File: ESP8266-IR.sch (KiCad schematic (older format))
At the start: 7 parts

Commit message: Initial commit.
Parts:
- added C4: 10uF, Capacitors_ThroughHole:C_Disc_D7.5_P5, symbol C
- added D1, D2, D3, D4: LED, LEDs:LED-5MM, symbol LED
- added IC1: ATTINY85-P, Housings_DIP:DIP-8_W7.62mm_LongPads, symbol ATTINY85-P
- added JP1, JP2: Jumper_NO_Small, Pin_Headers:Pin_Header_Straight_1x02, symbol Jumper_NO_Small
- added P1: CONN_01X06, Pin_Headers:Pin_Header_Straight_1x06, symbol CONN_01X06
- added Q1, Q2: 2N2222A, TO_SOT_Packages_THT:TO-18_3Pin, symbol Q_NPN_EBC
- added R1, R4: 10k, Resistors_ThroughHole:Resistor_Horizontal_RM10mm, symbol R
- added SW1, SW2, SW3: SW_PUSH, Custom:PushbuttonSquare2pin, symbol SW_PUSH
- C1, C2: renamed from C?; footprint (none) -> Capacitors_ThroughHole:C_Disc_D7.5_P5
- CON1: renamed from CON?; footprint (none) -> Connect:BARREL_JACK
- R2, R3: renamed from R?; footprint (none) -> Resistors_ThroughHole:Resistor_Horizontal_RM10mm
- U1: renamed from U?; footprint SOT-223 -> TO_SOT_Packages_THT:TO-220_Neutral123_Horizontal_LargePads
- U2: renamed from U?; footprint (none) -> adafruit:ESP-12
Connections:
- net +3V3: now also C4.2, D1.2 (A), D2.2 (A), D3.2 (A), D4.2 (A), JP1.1, JP2.1, P1.4 (P4), R1.1; no longer U2.8 (VCC)
- net ESP_RST: now also R1.2, SW3.2
- net ESP_RXD: now also P1.3 (P3)
- net ESP_TXD: now also P1.2 (P2)
- net GND: now also C4.1, IC1.4 (GND), P1.6 (P6), Q1.1 (E), Q2.1 (E), R4.2, SW1.1, SW2.1, SW3.1
- net GPIO0: now also SW2.2
- net VIN: now reaches C1.1, CON1.1, U1.3 (VI)
- net GPIO12: no longer names the net of U2.6 (GPIO12)
- net GPIO13: no longer names the net of U2.7 (GPIO13)
- net GPIO15: no longer names the net of U2.10 (GPIO15)
- net GPIO15: now also R4.1
- new net: JP2.2, U2.8 (VCC)
- new net: IC1.8 (VCC), JP1.2
- new net: D1.1 (K), D2.1 (K), Q1.3 (C)
- new net: D3.1 (K), D4.1 (K), Q2.3 (C)
- new net ATT_RST: IC1.1 (PB5(~RESET~/dW/ADC0/PCINT5)), SW1.2
- new net IR_OUT: IC1.6 (PB1(MISO/DO/AIN1/OC0B/OC1A/PCINT1)), Q1.2 (B), Q2.2 (B)
- no-connect marks 0 -> 1
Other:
- moved on the sheet: R2, R3, U2

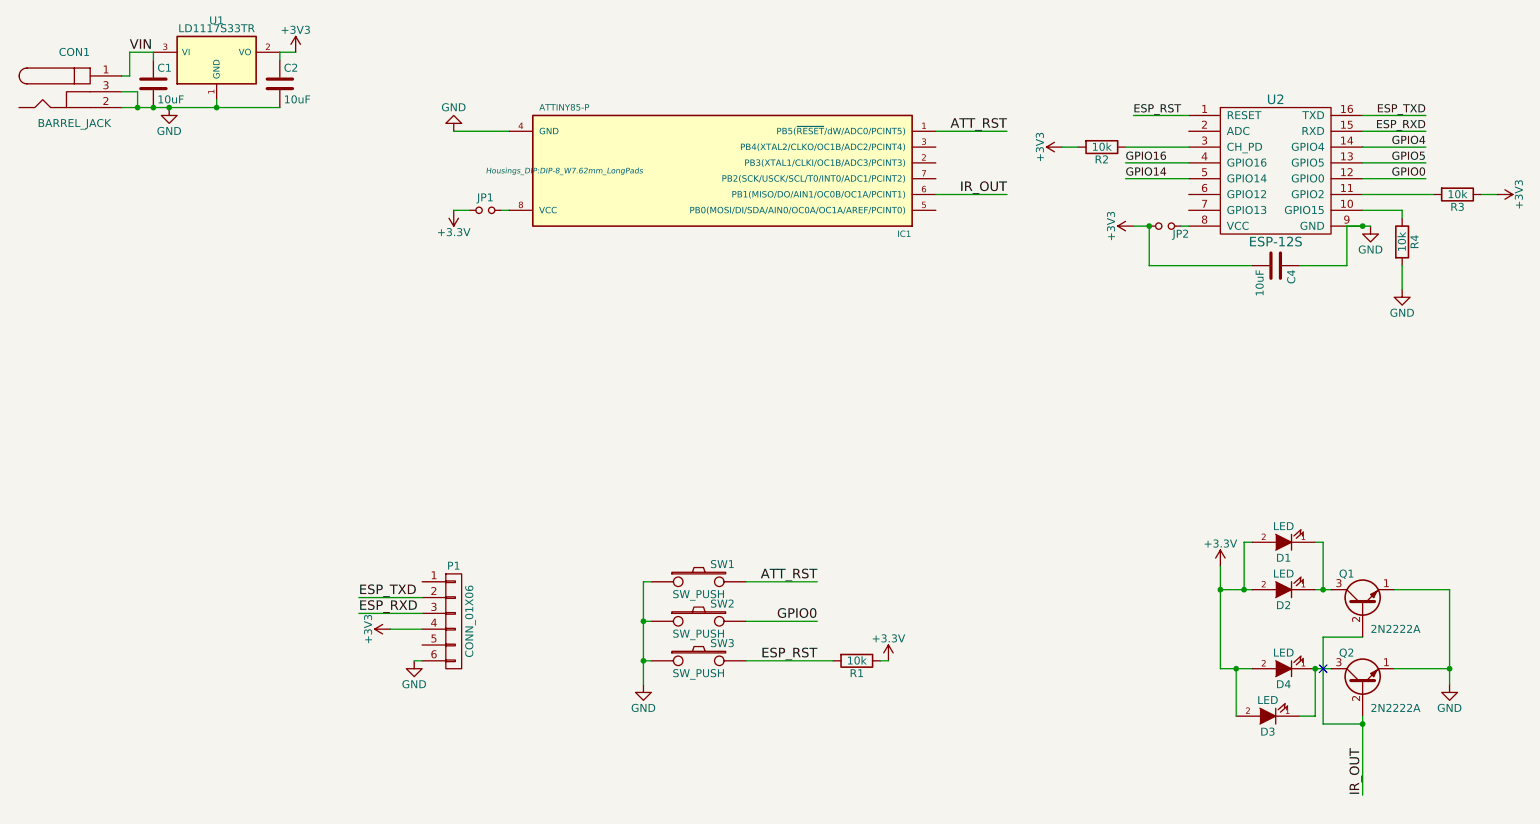
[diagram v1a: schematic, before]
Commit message: Removed ATTINY coprocessor.
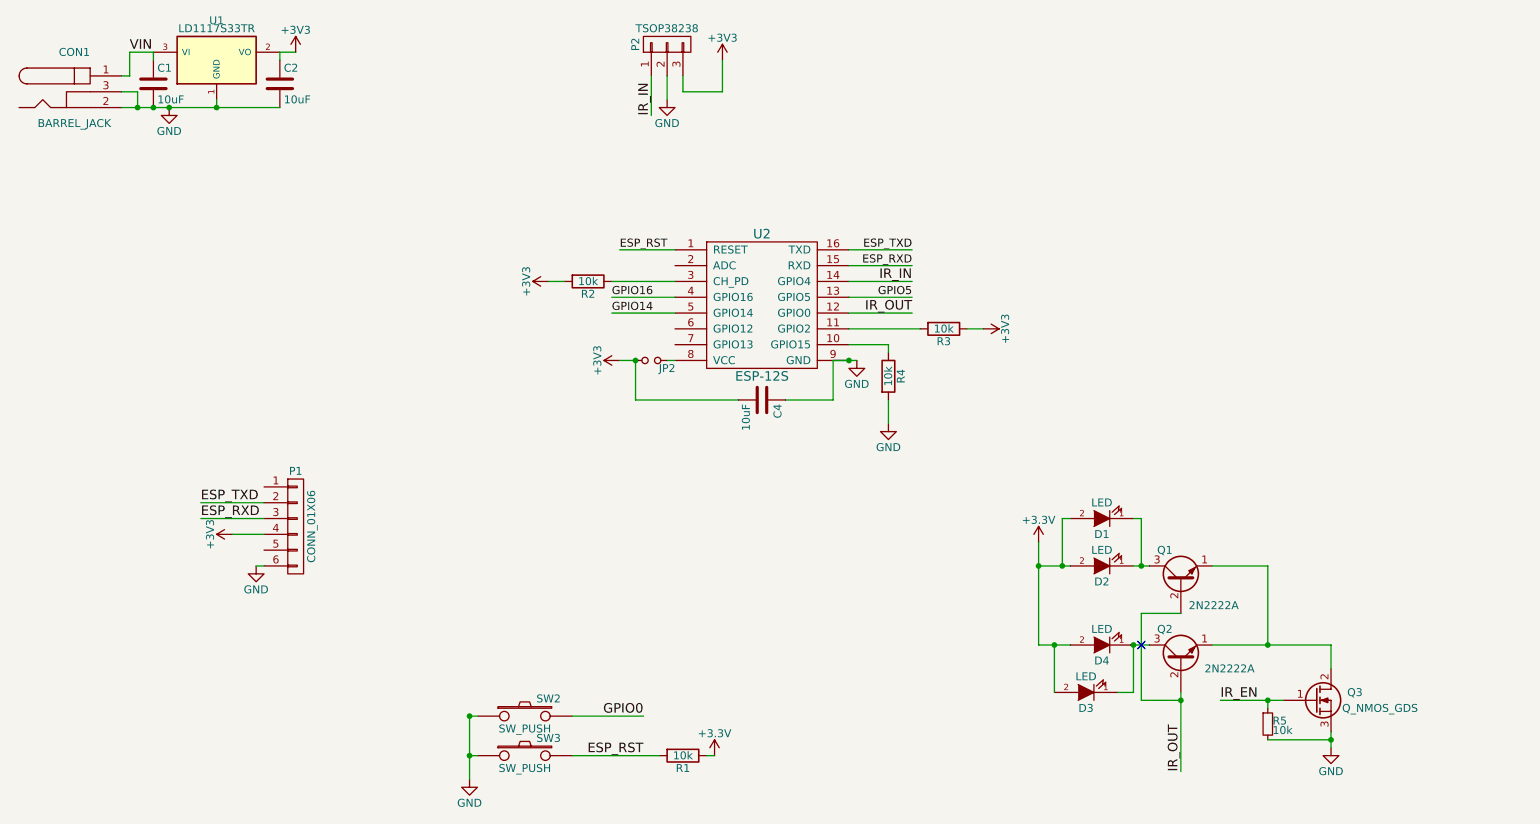
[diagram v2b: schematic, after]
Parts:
- removed IC1: ATTINY85-P, Housings_DIP:DIP-8_W7.62mm_LongPads, symbol ATTINY85-P
- removed JP1: Jumper_NO_Small, Pin_Headers:Pin_Header_Straight_1x02, symbol Jumper_NO_Small
- removed SW1: SW_PUSH, Custom:PushbuttonSquare2pin, symbol SW_PUSH
- added P2: TSOP38238, symbol CONN_01X03
- added Q3: Q_NMOS_GDS, symbol Q_NMOS_GDS
- added R5: 10k, symbol R_Small
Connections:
- net +3V3: now also P2.3 (P3)
- net GND: now also P2.2 (P2), Q3.3 (S), R5.2; no longer Q1.1 (E), Q2.1 (E)
- net GPIO0: no longer U2.12 (GPIO0)
- net IR_OUT: now also U2.12 (GPIO0)
- net GPIO4 renamed IR_IN
- net IR_IN: now also P2.1 (P1)
- new net: Q1.1 (E), Q2.1 (E), Q3.2 (D)
- new net IR_EN: Q3.1 (G), R5.1
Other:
- moved on the sheet: C4, D1, D2, D3, D4, JP2, P1, Q1, Q2, R1, R2, R3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

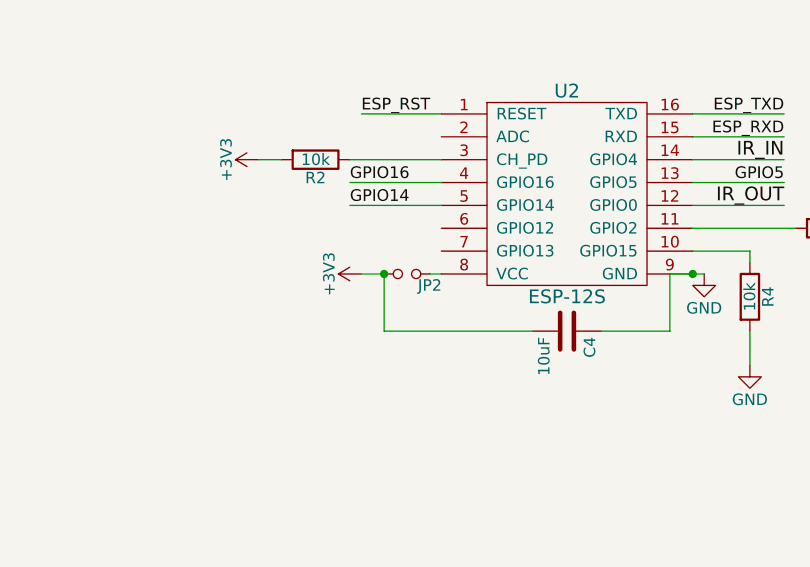
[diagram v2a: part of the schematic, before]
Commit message: Changed footpints.
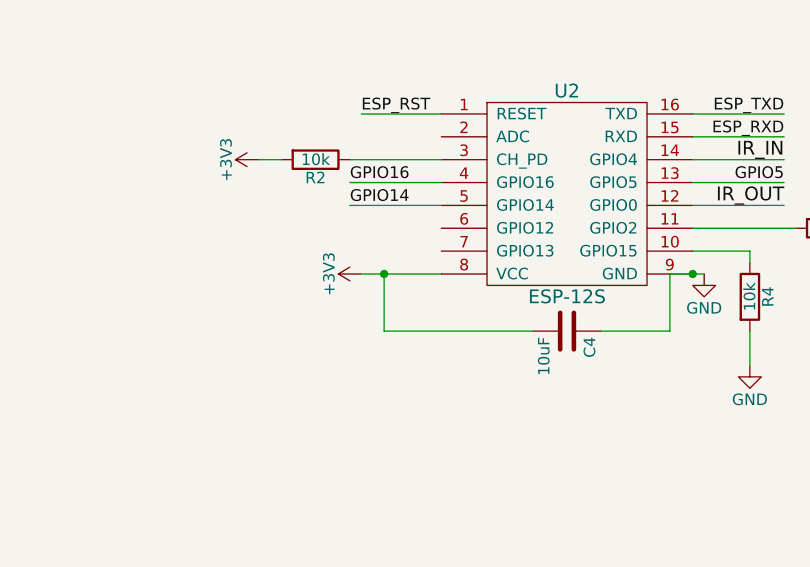
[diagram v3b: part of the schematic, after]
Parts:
- removed JP2: Jumper_NO_Small, Pin_Headers:Pin_Header_Straight_1x02, symbol Jumper_NO_Small
- C1, C2, C4: footprint Capacitors_ThroughHole:C_Disc_D7.5_P5 -> Capacitors_SMD:C_1206
- P2: footprint (none) -> Pin_Headers:Pin_Header_Straight_1x03
- Q3: footprint (none) -> Custom:SOT-223
- R1, R2, R3, R4: footprint Resistors_ThroughHole:Resistor_Horizontal_RM10mm -> Resistors_SMD:R_1206
- R5: footprint (none) -> Resistors_SMD:R_1206
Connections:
- net +3V3: now also U2.8 (VCC)
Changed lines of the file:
@@
 $EndComp
 $Comp
-L GND #PWR8
+L GND #PWR01
 U 1 1 584AEB9D
 P 6150 2950
-F 0 "#PWR8" H 6150 2700 50  0001 C CNN
+F 0 "#PWR01" H 6150 2700 50  0001 C CNN
 F 1 "GND" H 6150 2800 50  0000 C CNN
 F 2 "" H 6150 2950 50  0000 C CNN
@@
 $EndComp
 $Comp
-L +3V3 #PWR7
+L +3V3 #PWR02
 U 1 1 584AEBB3
 P 4650 2950
-F 0 "#PWR7" H 4650 2800 50  0001 C CNN
+F 0 "#PWR02" H 4650 2800 50  0001 C CNN
 F 1 "+3V3" H 4650 3090 50  0000 C CNN
 F 2 "" H 4650 2950 50  0000 C CNN
@@
 F 0 "R2" V 4530 2450 50  0000 C CNN
 F 1 "10k" V 4450 2450 50  0000 C CNN
-F 2 "Resistors_ThroughHole:Resistor_Horizontal_RM10mm" V 4380 2450 50  0001 C CNN
+F 2 "Resistors_SMD:R_1206" V 4380 2450 50  0001 C CNN
 F 3 "" H 4450 2450 50  0000 C CNN
 	1    4450 2450
@@
 $EndComp
 $Comp
-L +3V3 #PWR5
+L +3V3 #PWR03
 U 1 1 584AEC43
 P 4200 2450
-F 0 "#PWR5" H 4200 2300 50  0001 C CNN
+F 0 "#PWR03" H 4200 2300 50  0001 C CNN
 F 1 "+3V3" H 4200 2590 50  0000 C CNN
 F 2 "" H 4200 2450 50  0000 C CNN
@@
 F 0 "R3" V 6780 2750 50  0000 C CNN
 F 1 "10k" V 6700 2750 50  0000 C CNN
-F 2 "Resistors_ThroughHole:Resistor_Horizontal_RM10mm" V 6630 2750 50  0001 C CNN
+F 2 "Resistors_SMD:R_1206" V 6630 2750 50  0001 C CNN
 F 3 "" H 6700 2750 50  0000 C CNN
 	1    6700 2750
@@
 $EndComp
 $Comp
-L +3V3 #PWR6
+L +3V3 #PWR04
 U 1 1 584AECDE
 P 6950 2750
-F 0 "#PWR6" H 6950 2600 50  0001 C CNN
+F 0 "#PWR04" H 6950 2600 50  0001 C CNN
 F 1 "+3V3" H 6950 2890 50  0000 C CNN
 F 2 "" H 6950 2750 50  0000 C CNN
@@
 $EndComp
 $Comp
-L +3V3 #PWR1
+L +3V3 #PWR05
 U 1 1 584B2A57
 P 2600 1000
-F 0 "#PWR1" H 2600 850 50  0001 C CNN
+F 0 "#PWR05" H 2600 850 50  0001 C CNN
 F 1 "+3V3" H 2600 1140 50  0000 C CNN
 F 2 "" H 2600 1000 50  0000 C CNN
@@
 $EndComp
 $Comp
-L GND #PWR4
+L GND #PWR06
 U 1 1 584B2A8E
 P 1800 1350
-F 0 "#PWR4" H 1800 1100 50  0001 C CNN
+F 0 "#PWR06" H 1800 1100 50  0001 C CNN
 F 1 "GND" H 1800 1200 50  0000 C CNN
 F 2 "" H 1800 1350 50  0000 C CNN
@@
 F 0 "C1" H 1725 1300 50  0000 L CNN
 F 1 "10uF" H 1725 1100 50  0000 L CNN
-F 2 "Capacitors_ThroughHole:C_Disc_D7.5_P5" H 1738 1050 50  0001 C CNN
+F 2 "Capacitors_SMD:C_1206" H 1738 1050 50  0001 C CNN
 F 3 "" H 1700 1200 50  0000 C CNN
 	1    1700 1200
@@
 F 0 "C2" H 2525 1300 50  0000 L CNN
 F 1 "10uF" H 2525 1100 50  0000 L CNN
-F 2 "Capacitors_ThroughHole:C_Disc_D7.5_P5" H 2538 1050 50  0001 C CNN
+F 2 "Capacitors_SMD:C_1206" H 2538 1050 50  0001 C CNN
 F 3 "" H 2500 1200 50  0000 C CNN
 	1    2500 1200
@@
 $EndComp
 $Comp
-L GND #PWR15
+L GND #PWR07
 U 1 1 584B6DE3
 P 3700 5600
-F 0 "#PWR15" H 3700 5350 50  0001 C CNN
+F 0 "#PWR07" H 3700 5350 50  0001 C CNN
 F 1 "GND" H 3700 5450 50  0000 C CNN
 F 2 "" H 3700 5600 60  0000 C CNN
@@
 F 0 "R1" V 5130 5450 50  0000 C CNN
 F 1 "10k" V 5050 5450 50  0000 C CNN
-F 2 "Resistors_ThroughHole:Resistor_Horizontal_RM10mm" V 4980 5450 30  0001 C CNN
+F 2 "Resistors_SMD:R_1206" V 4980 5450 30  0001 C CNN
 F 3 "" H 5050 5450 30  0000 C CNN
 	1    5050 5450
@@
 $EndComp
 $Comp
-L +3.3V #PWR14
+L +3.3V #PWR08
 U 1 1 584B735B
 P 5250 5450
-F 0 "#PWR14" H 5250 5300 50  0001 C CNN
+F 0 "#PWR08" H 5250 5300 50  0001 C CNN
 F 1 "+3.3V" H 5250 5590 50  0000 C CNN
 F 2 "" H 5250 5450 60  0000 C CNN
@@
 F 0 "C4" H 5575 3300 50  0000 L CNN
 F 1 "10uF" H 5575 3100 50  0000 L CNN
-F 2 "Capacitors_ThroughHole:C_Disc_D7.5_P5" H 5588 3050 30  0001 C CNN
+F 2 "Capacitors_SMD:C_1206" H 5588 3050 30  0001 C CNN
 F 3 "" H 5550 3200 60  0000 C CNN
 	1    5550 3200
@@
 Connection ~ 4750 2950
 $Comp
-L GND #PWR9
+L GND #PWR09
 U 1 1 584BB1BB
 P 6350 3350
-F 0 "#PWR9" H 6350 3100 50  0001 C CNN
+F 0 "#PWR09" H 6350 3100 50  0001 C CNN
 F 1 "GND" H 6350 3200 50  0000 C CNN
 F 2 "" H 6350 3350 60  0000 C CNN
@@
 F 0 "R4" V 6430 3050 50  0000 C CNN
 F 1 "10k" V 6350 3050 50  0000 C CNN
-F 2 "Resistors_ThroughHole:Resistor_Horizontal_RM10mm" V 6280 3050 30  0001 C CNN
+F 2 "Resistors_SMD:R_1206" V 6280 3050 30  0001 C CNN
 F 3 "" H 6350 3050 30  0000 C CNN
 	1    6350 3050
@@
 $EndComp
 $Comp
-L GND #PWR12
+L GND #PWR010
 U 1 1 584BD657
 P 2350 4250
-F 0 "#PWR12" H 2350 4000 50  0001 C CNN
+F 0 "#PWR010" H 2350 4000 50  0001 C CNN
 F 1 "GND" H 2350 4100 50  0000 C CNN
 F 2 "" H 2350 4250 60  0000 C CNN
@@
 $EndComp
 $Comp
-L GND #PWR13
+L GND #PWR011
 U 1 1 584C0476
 P 9150 5400
-F 0 "#PWR13" H 9150 5150 50  0001 C CNN
+F 0 "#PWR011" H 9150 5150 50  0001 C CNN
 F 1 "GND" H 9150 5250 50  0000 C CNN
 F 2 "" H 9150 5400 60  0000 C CNN
@@
 Connection ~ 7300 4250
 $Comp
-L +3.3V #PWR11
+L +3.3V #PWR012
 U 1 1 584C07AE
 P 7300 4100
-F 0 "#PWR11" H 7300 3950 50  0001 C CNN
+F 0 "#PWR012" H 7300 3950 50  0001 C CNN
 F 1 "+3.3V" H 7300 4240 50  0000 C CNN
 F 2 "" H 7300 4100 60  0000 C CNN
@@
 Text Label 8200 5550 1    60   ~ 0
 IR_OUT
-$Comp
-L Jumper_NO_Small JP2
-U 1 1 584C62D5
-P 4850 2950
-F 0 "JP2" H 4950 2900 50  0000 C CNN
-F 1 "Jumper_NO_Small" H 4860 2890 50  0001 C CNN
-F 2 "Pin_Headers:Pin_Header_Straight_1x02" H 4850 2950 60  0001 C CNN
-F 3 "" H 4850 2950 60  0000 C CNN
-	1    4850 2950
-	1    0    0    -1
-$EndComp
-Wire Wire Line
-	4650 2950 4750 2950
+Wire Wire Line
+	4650 2950 5000 2950
 Wire Wire Line
 	4750 2950 4750 3200
-Wire Wire Line
-	4950 2950 5000 2950
 Wire Wire Line
 	7950 4250 7950 3950
@@
 $EndComp
 $Comp
-L +3V3 #PWR10
+L +3V3 #PWR013
 U 1 1 584E0D51
 P 2200 4050
-F 0 "#PWR10" H 2200 3900 50  0001 C CNN
+F 0 "#PWR013" H 2200 3900 50  0001 C CNN
 F 1 "+3V3" H 2200 4190 50  0000 C CNN
 F 2 "" H 2200 4050 60  0000 C CNN
@@
 F 0 "P2" H 4950 1150 50  0000 C CNN
 F 1 "TSOP38238" V 5050 950 50  0000 C CNN
-F 2 "" H 4950 950 60  0000 C CNN
+F 2 "Pin_Headers:Pin_Header_Straight_1x03" H 4950 950 60  0001 C CNN
 F 3 "" H 4950 950 60  0000 C CNN
 	1    4950 950
@@
 $EndComp
 $Comp
-L GND #PWR3
+L GND #PWR014
 U 1 1 5852B3AF
 P 4950 1300
-F 0 "#PWR3" H 4950 1050 50  0001 C CNN
+F 0 "#PWR014" H 4950 1050 50  0001 C CNN
 F 1 "GND" H 4950 1150 50  0000 C CNN
 F 2 "" H 4950 1300 60  0000 C CNN
@@
 $EndComp
 $Comp
-L +3V3 #PWR2
+L +3V3 #PWR015
 U 1 1 5852B5BB
 P 5300 1050
-F 0 "#PWR2" H 5300 900 50  0001 C CNN
+F 0 "#PWR015" H 5300 900 50  0001 C CNN
 F 1 "+3V3" H 5300 1190 50  0000 C CNN
 F 2 "" H 5300 1050 60  0000 C CNN
@@
 F 0 "Q3" H 9350 5150 50  0000 R CNN
 F 1 "Q_NMOS_GDS" H 9700 5050 50  0000 R CNN
-F 2 "" H 9250 5200 29  0000 C CNN
+F 2 "Custom:SOT-223" H 9250 5200 29  0001 C CNN
 F 3 "" H 9050 5100 60  0000 C CNN
 	1    9050 5100
@@
 F 0 "R5" H 8780 5270 50  0000 L CNN
 F 1 "10k" H 8780 5210 50  0000 L CNN
-F 2 "" H 8750 5250 60  0000 C CNN
+F 2 "Resistors_SMD:R_1206" H 8750 5250 60  0001 C CNN
 F 3 "" H 8750 5250 60  0000 C CNN
 	1    8750 5250

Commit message: Complete relayout, more smoothing, two layer design.
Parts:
- added C3, C5: C, Capacitors_SMD:C_1206, symbol C
- P1: value CONN_01X06 -> CONN_01X05; footprint Pin_Headers:Pin_Header_Straight_1x06 -> Pin_Headers:Pin_Header_Straight_1x05; symbol CONN_01X06 -> CONN_01X05
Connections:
- net GPIO14 is gone; now on net IR_EN: U2.5 (GPIO14)
- net GPIO16 is gone; now on net IR_IN: U2.4 (GPIO16)
- net IR_OUT is gone; now on net GPIO0: Q1.2 (B), Q2.2 (B), U2.12 (GPIO0)
- net +3V3: now also P1.3 (P3), C3.1, C5.1; no longer P1.4 (P4)
- net ESP_RXD: now also P1.2 (P2); no longer P1.3 (P3)
- net ESP_TXD: now also P1.1 (P1); no longer P1.2 (P2)
- net GND: now also P1.5 (P5), C3.2, C5.2; no longer P1.6 (P6)
- net IR_IN: no longer U2.14 (GPIO4)
- net GPIO5: no longer names the net of U2.13 (GPIO5)
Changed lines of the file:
@@
 	1    0    0    -1
 $EndComp
-Text Label 6500 2550 2    51   ~ 0
-GPIO5
-Text Label 4600 2650 0    51   ~ 0
-GPIO14
-Text Label 4600 2550 0    51   ~ 0
-GPIO16
 $Comp
 L SW_PUSH SW2
@@
 Connection ~ 1700 1350
 Wire Wire Line
-	6100 2450 6500 2450
-Wire Wire Line
-	6500 2550 6100 2550
-Wire Wire Line
-	6100 2650 6500 2650
-Wire Wire Line
-	4600 2650 5000 2650
-Wire Wire Line
-	5000 2550 4600 2550
+	6100 2650 6800 2650
 Wire Wire Line
 	3750 5200 3700 5200
@@
 	6350 3200 6350 3350
 $Comp
-L CONN_01X06 P1
+L CONN_01X05 P1
 U 1 1 584BB4C5
-P 2600 4000
-F 0 "P1" H 2600 4350 50  0000 C CNN
-F 1 "CONN_01X06" V 2700 4000 50  0000 C CNN
-F 2 "Pin_Headers:Pin_Header_Straight_1x06" H 2600 4000 60  0001 C CNN
-F 3 "" H 2600 4000 60  0000 C CNN
-	1    2600 4000
+P 2600 4050
+F 0 "P1" H 2600 4400 50  0000 C CNN
+F 1 "CONN_01X05" V 2700 4050 50  0000 C CNN
+F 2 "Pin_Headers:Pin_Header_Straight_1x05" H 2600 4050 60  0001 C CNN
+F 3 "" H 2600 4050 60  0000 C CNN
+	1    2600 4050
 	1    0    0    -1
 $EndComp
@@
 	7300 4750 7500 4750
 Wire Wire Line
-	7300 4750 7300 4100
+	7300 4100 7300 4750
 Connection ~ 7300 4250
 $Comp
@@
 Wire Wire Line
 	4850 1400 4850 1150
-Text Label 6500 2450 2    60   ~ 0
-IR_IN
 $Comp
 L Q_NMOS_GDS Q3
@@
 	8750 5350 9150 5350
 Connection ~ 9150 5350
-Text Label 6500 2650 2    60   ~ 0
+Text Label 6500 2650 2    49   ~ 0
 IR_OUT
+Text Label 6800 2650 2    49   ~ 0
+GPIO0
+Text Label 4750 2650 0    49   ~ 0
+IR_EN
+Text Label 4750 2550 0    49   ~ 0
+IR_IN
+Wire Wire Line
+	4750 2550 5000 2550
+Wire Wire Line
+	5000 2650 4750 2650
+$Comp
+L C C3
+U 1 1 585DBBBC
+P 8850 1700
+F 0 "C3" H 8875 1800 50  0000 L CNN
+F 1 "C" H 8875 1600 50  0000 L CNN
+F 2 "Capacitors_SMD:C_1206" H 8888 1550 30  0001 C CNN
+F 3 "" H 8850 1700 60  0000 C CNN
+	1    8850 1700
+	1    0    0    -1
+$EndComp
+$Comp
+L C C5
+U 1 1 585DBCBA
+P 9050 1700
+F 0 "C5" H 9075 1800 50  0000 L CNN
+F 1 "C" H 9075 1600 50  0000 L CNN
+F 2 "Capacitors_SMD:C_1206" H 9088 1550 30  0001 C CNN
+F 3 "" H 9050 1700 60  0000 C CNN
+	1    9050 1700
+	1    0    0    -1
+$EndComp
+$Comp
+L GND #PWR016
+U 1 1 585DBD00
+P 9050 1950
+F 0 "#PWR016" H 9050 1700 50  0001 C CNN
+F 1 "GND" H 9050 1800 50  0000 C CNN
+F 2 "" H 9050 1950 60  0000 C CNN
+F 3 "" H 9050 1950 60  0000 C CNN
+	1    9050 1950
+	1    0    0    -1
+$EndComp
+$Comp
+L +3V3 #PWR017
+U 1 1 585DBF63
+P 9050 1450
+F 0 "#PWR017" H 9050 1300 50  0001 C CNN
+F 1 "+3V3" H 9050 1590 50  0000 C CNN
+F 2 "" H 9050 1450 60  0000 C CNN
+F 3 "" H 9050 1450 60  0000 C CNN
+	1    9050 1450
+	1    0    0    -1
+$EndComp
+Wire Wire Line
+	8850 1850 8850 1900
+Wire Wire Line
+	8850 1900 9050 1900
+Wire Wire Line
+	9050 1850 9050 1950
+Connection ~ 9050 1900
+Wire Wire Line
+	9050 1550 9050 1450
+Wire Wire Line
+	8850 1550 8850 1500
+Wire Wire Line
+	8850 1500 9050 1500
+Connection ~ 9050 1500
 $EndSCHEMATC
